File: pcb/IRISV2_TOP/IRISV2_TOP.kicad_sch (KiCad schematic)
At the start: 12 parts, among them J2 USB_C_Receptacle_USB2.0_16P, J3 USB_C_Receptacle_USB2.0_16P

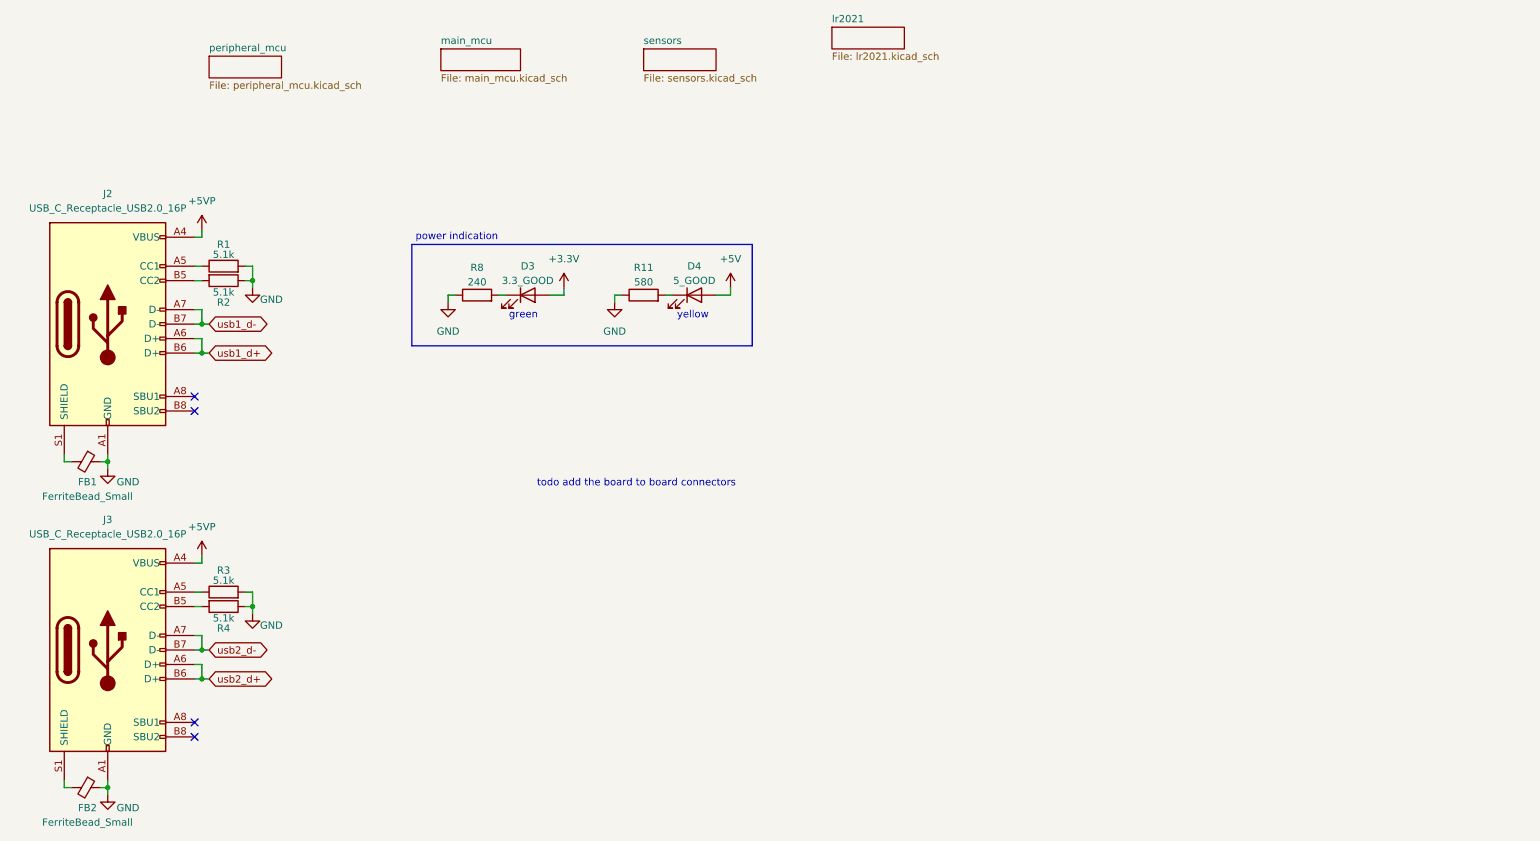
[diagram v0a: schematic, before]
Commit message: gps finished minus tvs (WHY ARE THEY ALL 0201), top layout + routing started
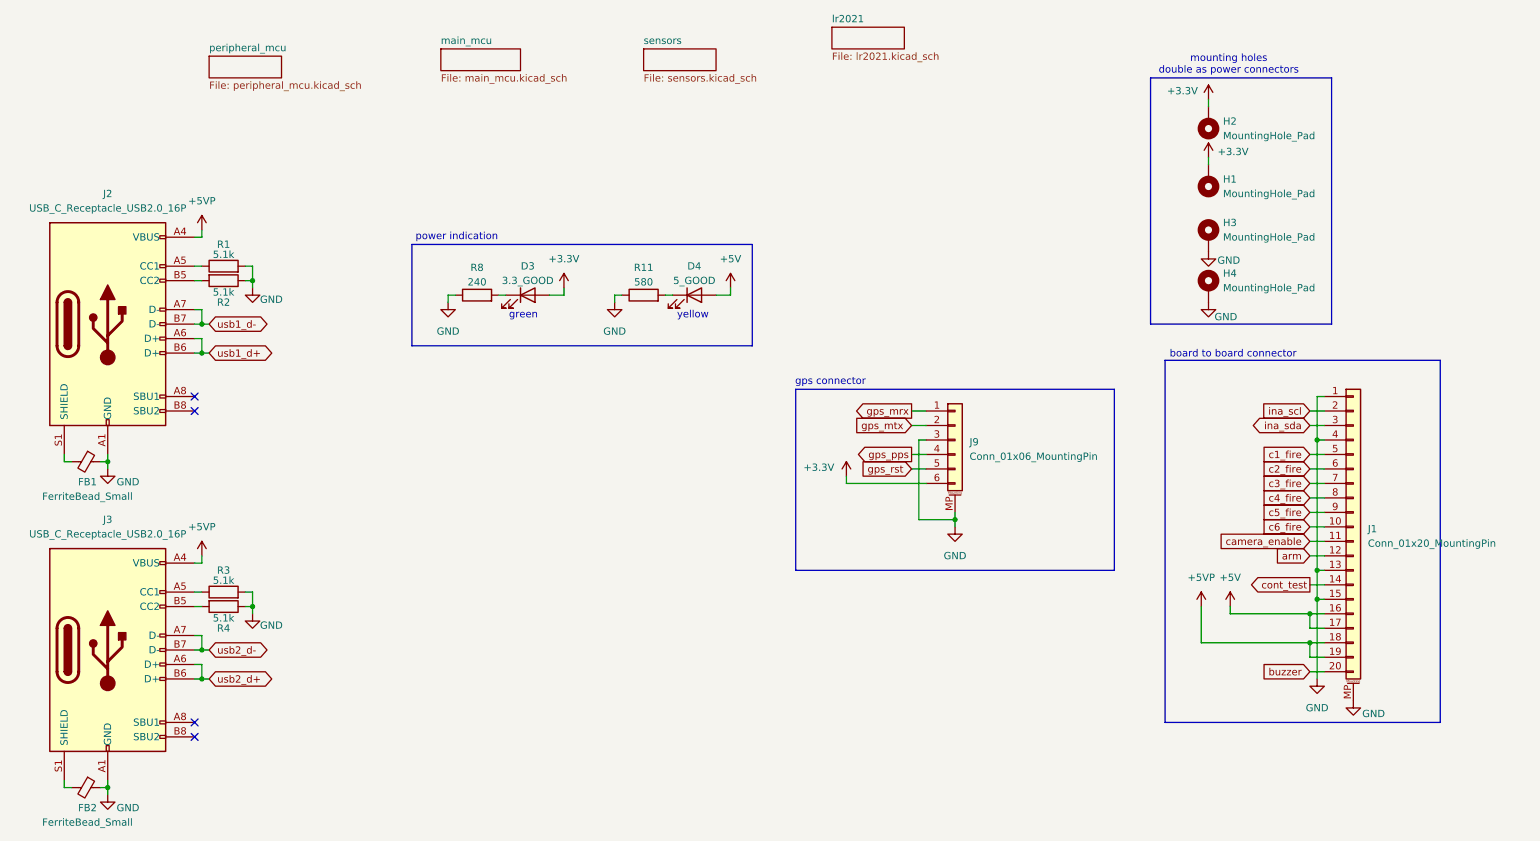
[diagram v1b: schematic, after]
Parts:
- added H1, H2, H3, H4: MountingHole_Pad, MountingHole:MountingHole_3.2mm_M3_ISO7380_Pad_TopBottom, symbol Mechanical:MountingHole_Pad
- added J1: Conn_01x20_MountingPin, FFC3B07-20-T:FFC3B07-20-T, symbol Connector_Generic_MountingPin:Conn_01x20_MountingPin
- added J9: Conn_01x06_MountingPin, Connector_JST:JST_PH_S6B-PH-SM4-TB_1x06-1MP_P2.00mm_Horizontal, symbol Connector_Generic_MountingPin:Conn_01x06_MountingPin
- D3, D4: footprint (none) -> LED_SMD:LED_0805_2012Metric
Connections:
- net +3.3V: now also H1.1, H2.1, J9.6 (Pin_6)
- net +5V: now also J1.16 (Pin_16), J1.17 (Pin_17)
- net +5VP: now also J1.18 (Pin_18), J1.19 (Pin_19)
- net GND: now also H3.1, H4.1, J1.1 (Pin_1), J1.13 (Pin_13), J1.15 (Pin_15), J1.4 (Pin_4), J1.MP (MountPin), J9.3 (Pin_3), J9.MP (MountPin)
- new net arm: J1.12 (Pin_12)
- new net buzzer: J1.20 (Pin_20)
- new net c1_fire: J1.5 (Pin_5)
- new net c2_fire: J1.6 (Pin_6)
- new net c3_fire: J1.7 (Pin_7)
- new net c4_fire: J1.8 (Pin_8)
- new net c5_fire: J1.9 (Pin_9)
- new net c6_fire: J1.10 (Pin_10)
- new net camera_enable: J1.11 (Pin_11)
- new net cont_test: J1.14 (Pin_14)
- new net gps_mrx: J9.1 (Pin_1)
- new net gps_mtx: J9.2 (Pin_2)
- new net gps_pps: J9.4 (Pin_4)
- new net gps_rst: J9.5 (Pin_5)
- new net ina_scl: J1.2 (Pin_2)
- new net ina_sda: J1.3 (Pin_3)
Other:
- note added: "board to board connector"
- note added: "gps connector"
- note added: "mounting holes double as power connectors"
- note removed: "todo add the board to board connectors"

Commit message: removed high g accel, top board layout looking decent, routing started also - though i realized i was missing the micro sd card and that's going to be a pain to add
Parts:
- FB1, FB2: footprint (none) -> Inductor_SMD:L_0402_1005Metric
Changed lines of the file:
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@@
 			)
 		)
-		(property "Footprint" ""
+		(property "Footprint" "Inductor_SMD:L_0402_1005Metric"
 			(at 29.21 102.362 90)
 			(effects
@@
 			)
 		)
-		(property "Footprint" ""
+		(property "Footprint" "Inductor_SMD:L_0402_1005Metric"
 			(at 29.21 159.512 90)
 			(effects
